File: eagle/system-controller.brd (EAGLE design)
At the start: 99 x 100 mm, 233 parts, among them J1 1, Q0 MOSFET-P-N-PAIR, Q1 MOSFET-P-N-PAIR, Q10 DNP/NTR4101P, Q12 DNP/NTR4101P, Q13 DON3035L, Q2 MOSFET-P-N-PAIR, Q3 MOSFET-P-N-PAIR, Q4 MOSFET-P-N-PAIR, Q5 MOSFET-P-N-PAIR, Q6 MOSFET-P-N-PAIR, Q7 MOSFET-P-N-PAIR, U1 MEGA128-A, U10 TPS25944LRVCRWQFN-20-3X4, U11 TPS25944LRVCRWQFN-20-3X4, U12 TPS25944LRVCRWQFN-20-3X4, U13 TPS25944LRVCRWQFN-20-3X4, U14 TPS25944LRVCRWQFN-20-3X4, U15 TS4100, U2 LP5907MFX-3.0, U3 ACPL-M61L, U4 ACPL-M61L, U5 ACPL-M61L, U6 ACPL-M61L, U7 TPS25944LRVCRWQFN-20-3X4, U8 TPS25944LRVCRWQFN-20-3X4, U9 TPS25944LRVCRWQFN-20-3X4, X1 8 MHz CRYSTAL-ABRACON-ABM3-SMD

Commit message: More board cleanup!
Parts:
- moved TP7GHT 63.7 mm to (78.2, 73.1)
- moved RIMON6 54.5 mm to (85.6, 30.4), turned to 90 degrees
- moved RIMON7 54.2 mm to (85.6, 20.9), turned to 90 degrees
- moved RIMON0 50.1 mm to (85.6, 87.4)
- moved RIMON4 49.9 mm to (85.6, 49.4), turned to 90 degrees
- moved RIMON2 49.0 mm to (85.6, 68.3)
- moved RIMON1 48.6 mm to (85.6, 77.9)
- moved RIMON5 44.8 mm to (85.6, 39.9), turned to 90 degrees
- moved RIMON3 39.7 mm to (85.6, 58.8)
- moved TPLDOA 15.3 mm to (38.9, 76.0)
- moved R60 13.3 mm to (37.2, 75.2), turned to 90 degrees
- moved C22 11.3 mm to (41.9, 76.5), turned to 0 degrees
- moved TP2GHT 9.89 mm to (78.2, 54.2)
- moved TP1GHT 9.82 mm to (77.7, 63.5)
- moved TP5GHT 9.42 mm to (77.3, 24.9)
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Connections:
- net GND: now also CF3.P$19, CF3.P$29, CF3.P$39, CF3.P$9; no longer CF3.P$15, CF3.P$25, CF3.P$35, CF3.P$5
- net VCB1: now also CF3.P$5; no longer CF3.P$9
- net VCB3: now also CF3.P$15; no longer CF3.P$19
- net VCB5: now also CF3.P$25; no longer CF3.P$29
- net VCB7: now also CF3.P$35; no longer CF3.P$39
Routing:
- net VCB7: track 39.0 -> 21.3 mm, vias 2 -> 1
- net V+: track 19.1 -> 8.18 mm, vias 0 -> 2
- net VCB2_IMON: track 68.8 -> 60.0 mm
- net VBUS: track 25.2 -> 16.7 mm, vias 32 -> 48
- net VCB5_IMON: track 70.9 -> 63.1 mm
- net 3V: track 55.9 -> 48.6 mm, vias 30 -> 35
- net GND: track 78.4 -> 71.6 mm, vias 278 -> 279
- net N$48: track 68.8 -> 62.6 mm
- net N$63: track 9.35 -> 3.61 mm
- net N$95: track 9.24 -> 3.61 mm
- net N$79: track 9.15 -> 3.71 mm
- net N$87: track 9.11 -> 3.81 mm
- net N$50: track 9.07 -> 3.81 mm
- net N$49: track 9.04 -> 3.81 mm
- net N$22: track 8.94 -> 3.72 mm
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
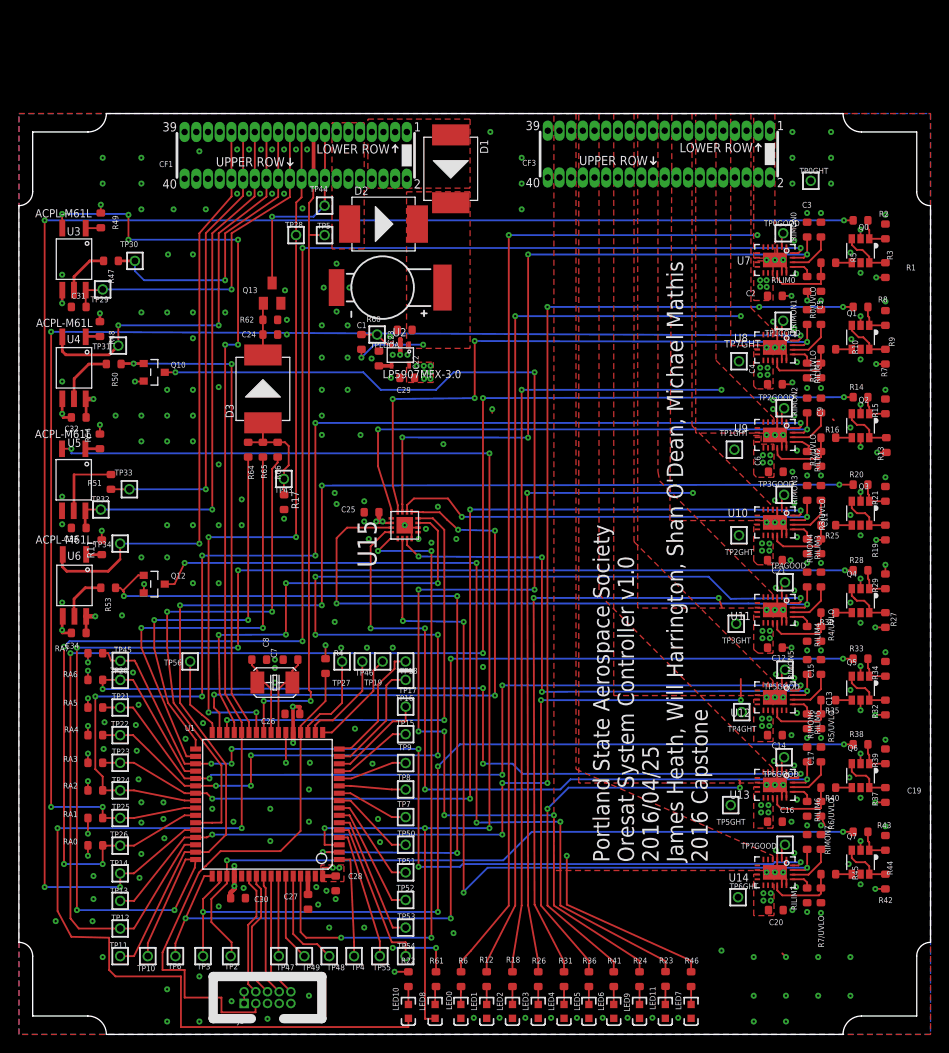
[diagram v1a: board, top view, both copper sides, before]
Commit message: Lots of board cleanup. Improved packages for ATMEGA, analog switch, and TPS. Re-did power polygons to tighten up the layout. Straightened wires because OCD, fixed DRCs.
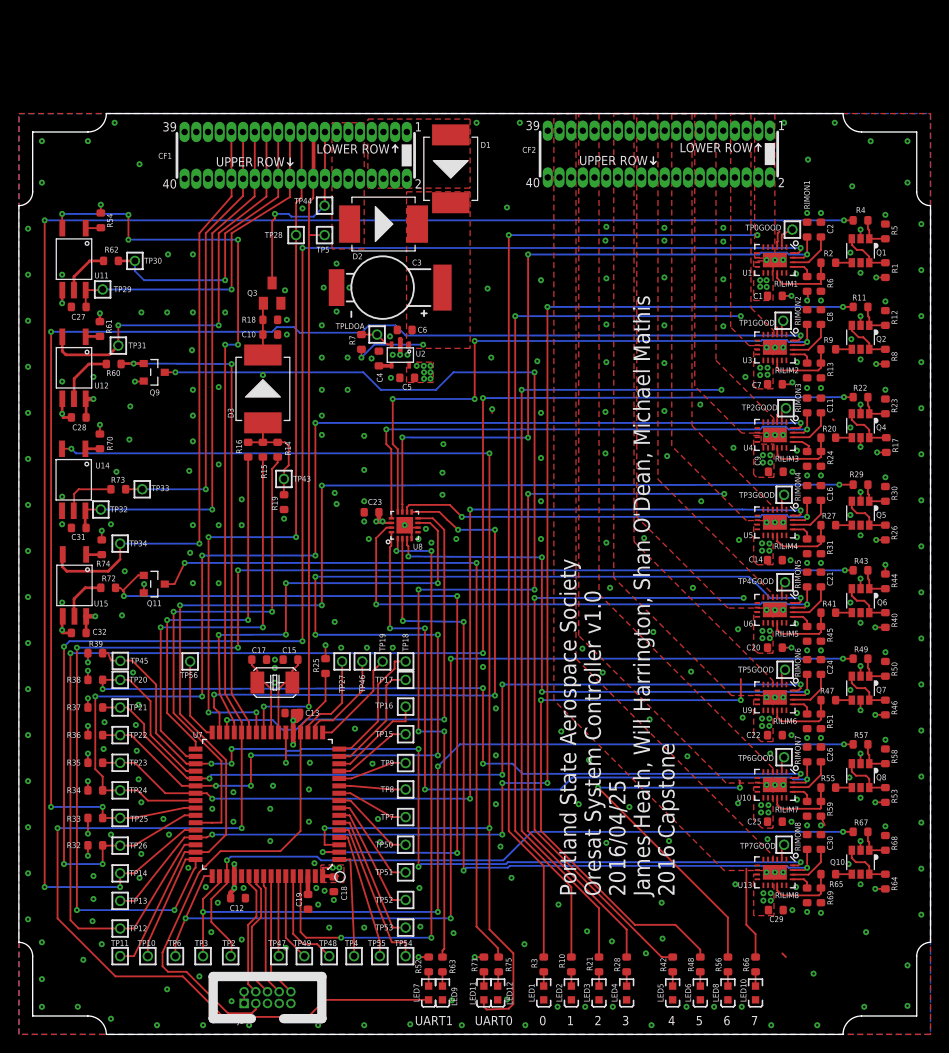
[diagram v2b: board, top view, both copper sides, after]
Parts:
- removed C33, C34: 100nF, rcl_custom:.0603-B-NOSILK
- removed LED0: DNP/GRN, psas_c3_team05:LED-0603
- removed Q0: MOSFET-P-N-PAIR, ic-transistor-mosfet-n-p:SOT23-6
- removed Q13: DON3035L, adafruit:SOT23
- removed R0/UVLO, R1/UVLO, R2/UVLO, R3/UVLO, R4/UVLO, R5/UVLO, RA0, RA1, RA2, RA3, RA4, RA5, RA6, RA7, RILIM0: 47k, rcl_custom:.0603-B-NOSILK
- removed RIMON0: 30k, rcl_custom:.0603-B-NOSILK
- removed TP0GHT, TP1GHT, TP2GHT, TP3GHT, TP4GHT, TP5GHT, TP6GHT, TP7GHT: TEST-POINT, Tova:2MM-TEST-POINT
- added C10: 22u, rcl_custom:.0603-B-NOSILK
- added C18: 100nF, rcl_custom:.0603-B-NOSILK
- added LED12: DNP/AMB, psas_c3_team05:LED-0603
- added Q8: MOSFET-P-N-PAIR, ic-transistor-mosfet-n-p:SOT23-6
- added Q9: DNP/NTR4101P, Tova:SOT23
- added R52, R56, R63, R71, R75: DNP/1k, rcl_custom:.0603-B-NOSILK
- added R55: 93.1k, rcl_custom:.0603-B-NOSILK
- added R57, R67: 4.7k, rcl_custom:.0603-B-NOSILK
- added R58, R68, RILIM8: 47k, rcl_custom:.0603-B-NOSILK
- added R70, R72, R74: 390, rcl_custom:.0603-B-NOSILK
- added R73: 1k, rcl_custom:.0603-B-NOSILK
- added RIMON8: 30k, rcl_custom:.0603-B-NOSILK
- C1: value CAP-ELNA-DS -> 1uF; device cap-elna-ds:CAP-ELNA-DS-SERIES -> rcl_custom:.0603-B-NOSILK
- C12: value 1uF -> 100nF
- C13, C19: value 2.2nF -> 100nF
- C15, C17: value 2.2nF -> 9pF
- C16, C2, C21: value 1uF -> 2.2nF
- C23: value 10nF -> 1uF
- C24: value 22u -> 2.2nF
- C26, C30: value 100nF -> 2.2nF
- C29: value 2.2uF -> 1uF
- C3: value 2.2nF -> CAP-ELNA-DS; device rcl_custom:.0603-B-NOSILK -> cap-elna-ds:CAP-ELNA-DS-SERIES
- C4: value 1uF -> 10nF
- C5: value 2.2nF -> 2.2uF
- C7: value 9pF -> 1uF
- C8: value 9pF -> 2.2nF
- C9: value 2.2nF -> 1uF
- D1, D2: value SMD-DIODE-SCHOTTKY-40V-5A(DO-214AB)-SSC53L -> SSC53L
- LED10, LED8: value DNP/AMB -> DNP/GRN
- LED7: value DNP/GRN -> DNP/AMB
- Q10: value DNP/NTR4101P -> MOSFET-P-N-PAIR; device Tova:SOT23 -> ic-transistor-mosfet-n-p:SOT23-6
- Q3: value MOSFET-P-N-PAIR -> DON3035L; device ic-transistor-mosfet-n-p:SOT23-6 -> adafruit:SOT23
- R10: value 93.1k -> DNP/1k
- R11, R4, R49: value 390 -> 4.7k
- R12, R23, R24, R26, R31, R36, R46, R6: value DNP/1k -> 47k
- R14: value 4.7k -> 390
- R15, R19: value 47k -> 390
- R16, R25: value 93.1k -> 390
- R17, R50, R51, R53, R64: value 390 -> 47k
- R18: value DNP/1k -> 470k
- R2, R20: value 4.7k -> 93.1k
- R21, R3, R42: value 47k -> DNP/1k
- R22: value DNP/1k -> 4.7k
- R27, R9: value 47k -> 93.1k
- R28: value 4.7k -> DNP/1k
- R29: value 47k -> 4.7k
- R30, R35, R40, R45, R5: value 93.1k -> 47k
- R33, R38, R8: value 4.7k -> 47k
- R41: value DNP/1k -> 93.1k
- R47, R65: value 390 -> 93.1k
- R48, R66: value 390 -> DNP/1k
- R60: value 10k -> 390
- R61: value DNP/1k -> 390
- R62: value 470k -> 1k
- R7: value 47k -> 10k
- U1: value MEGA128-A -> TPS25944LRVCRWQFN-20-3X4; device atmegas128:TQFP64 -> system-controller:QFN-20-L
- U11, U12, U14: value TPS25944LRVCRWQFN-20-3X4 -> ACPL-M61L; device system-controller:QFN-20-L -> system-controller:ACPL-M61L
- U15: value TS4100 -> ACPL-M61L; device system-controller:QFN50P400X400X80-17N -> system-controller:ACPL-M61L
- U3, U4, U5, U6: value ACPL-M61L -> TPS25944LRVCRWQFN-20-3X4; device system-controller:ACPL-M61L -> system-controller:QFN-20-L
- U7: value TPS25944LRVCRWQFN-20-3X4 -> ATMEGA128L-8A(U/N); device system-controller:QFN-20-L -> atmegas128:TQFP64
- U8: value TPS25944LRVCRWQFN-20-3X4 -> TS4100; device system-controller:QFN-20-L -> system-controller:QFN50P400X400X80-17N
- moved R49 95.2 mm to (91.4, 40.8), turned to 0 degrees
- moved R48 94.9 mm to (74.0, 7.60), turned to 270 degrees
- moved Q10 93.3 mm to (91.4, 18.7), turned to 0 degrees
- moved R47 91.3 mm to (87.9, 36.3)
- moved R50 90.1 mm to (94.1, 39.7), turned to 90 degrees
- moved R3 87.8 mm to (57.0, 7.60), turned to 270 degrees
- moved R53 87.3 mm to (94.1, 26.0), turned to 90 degrees
- moved U14 87.1 mm to (5.97, 59.9)
- moved R32 87.1 mm to (8.30, 20.5), turned to 0 degrees
- moved R34 86.8 mm to (8.30, 26.5), turned to 0 degrees
- moved R39 86.5 mm to (8.30, 41.4), turned to 0 degrees
- moved R11 86.4 mm to (91.4, 79.0), turned to 0 degrees
- moved R37 86.3 mm to (8.30, 35.5), turned to 0 degrees
- moved R6 85.0 mm to (87.1, 81.5)
- moved U11 85.0 mm to (6.00, 83.9)
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- renumbered CF3 to CF2, Q12 to Q11, R6/UVLO to R59, R7/UVLO to R69
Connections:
- net 3V: now also C12.2, C13.2, C18.2, C23.2, C5.1, Q9.2, R25.1, R32.1, R33.1, R34.1, R35.1, R36.1, R37.1, R38.1, R39.1, R52.1, R61.2, R70.2, R71.1, R74.2, U12.5, U15.5, U7.21, U7.52, U7.64, U8.14; no longer C25.2, C26.2, C29.1, C30.2, C34.2, Q10.2, R11.2, R22.1, R4.1, R48.2, R49.2, R61.1, RA0.1, RA1.1, RA2.1, RA3.1, RA4.1, RA5.1, RA6.1, RA7.1, U1.21, U1.52, U1.64, U15.14, U4.5, U6.5
- net AREF: now also C19.2, U7.62; no longer C27.2, U1.62
- net GND: now also C1.1, C10.2, C13.1, C15.1, C16.2, C17.1, C18.1, C19.1, C2.2, C21.2, C23.1, C26.2, C29.1, C3.-, C30.2, C4.2, C8.2, C9.1, LED10.K, LED12.K, LED8.K, Q10.5, Q3.2, Q8.5, R12.2, R13.2, R18.2, R19.2, R23.2, R24.2, R30.2, R31.2, R45.2, R5.2, R50.2, R51.2, R58.2, R6.2, R68.2, RILIM8.2, RIMON8.2, U1.1, U1.15, U1.16, U1.21, U1.3, U15.3, U3.1, U3.15, U3.16, U3.21, U4.1, U4.15, U4.16, U4.21, U5.1, U5.15, U5.16, U5.21, U6.1, U6.15, U6.16, U6.21, U7.22, U7.53, U7.63, U8.17, U8.4, U8.6; no longer C1.-, C13.2, C15.2, C16.1, C17.2, C19.2, C2.1, C21.1, C23.2, C26.1, C29.2, C3.2, C30.1, C33.1, C34.1, C4.1, C8.1, C9.2, LED0.K, LED11.K, LED7.K, Q0.5, Q13.2, Q3.5, R0/UVLO.2, R1/UVLO.2, R15.2, R17.2, R2/UVLO.2, R21.2, R29.2, R3.2, R3/UVLO.2, R34.2, R39.2, R4/UVLO.2, R5/UVLO.2, R62.2, R9.2, RILIM0.2, RIMON0.2, TP0GHT.1, TP1GHT.1, TP2GHT.1, TP3GHT.1, TP4GHT.1, TP5GHT.1, TP6GHT.1, TP7GHT.1, U1.22, U1.53, U1.63, U11.1, U11.15, U11.16, U11.21, U12.1, U12.15, U12.16, U12.21, U14.1, U14.15, U14.16, U14.21, U15.17, U15.4, U15.6, U7.1, U7.15, U7.16, U7.21, U7.3, U8.1, U8.15, U8.16, U8.21, U8.3
- net I2C-SCL: now also U7.25; no longer U1.25
- net I2C-SDA: now also U7.26; no longer U1.26
- net INOF: now also C2.1, U1.18; no longer C3.1, U7.18
- net N$1: now also C17.2, U7.24; no longer C8.2, U1.24
- net N$10: now also R20.2, R24.1, U4.14; no longer R16.2, R2/UVLO.1, U9.14
- net N$100: now also RILIM7.1, U10.17; no longer RILIM6.1, U13.17
- net N$101: now also U10.2; no longer U13.2
- net N$102: now also C26.1, U10.18; no longer C17.1, U13.18
- net N$103: now also Q8.1, R57.2, R58.1; no longer Q6.1, R38.2, R39.1
- net N$104: now also U7.32; no longer U1.32
- net N$105: now also Q8.3, Q8.6, R53.2; no longer Q6.3, Q6.6, R37.2
- net N$106: now also C10.1, Q3.1, R18.1; no longer C24.1, Q13.1, R62.1
- net N$107: now also U7.61, U8.1; no longer U1.61, U15.1
- net N$108: now also Q7.4, R47.1; no longer Q5.4, R35.1
- net N$109: now also R14.1, R15.1, R16.1, R19.1; no longer R17.1, R64.1, R65.1, R66.1
- net N$11: now also U7.57; no longer U1.57
- net N$110: now also Q10.4, R65.1; no longer Q7.4, R45.1
- net N$111: now also Q8.4, R55.1; no longer Q6.4, R40.1
- net N$12: now also U7.55; no longer U1.55
- net N$13: now also U7.56; no longer U1.56
- net N$14: now also U7.54; no longer U1.54
- net N$15: now also R25.2, U7.20; no longer R4.2, U1.20
- net N$16: now also R73.2, U14.4; no longer R51.2, U5.4
- net N$17: now also C15.2, U7.23; no longer C7.2, U1.23
- net N$18: now also R72.1, U15.4; no longer R53.1, U6.4
- net N$19: now also RILIM3.1, U4.17; no longer RILIM2.1, U9.17
- net N$2: now also Q2.4, R9.1; no longer Q1.4, R10.1
- net N$21: now also RILIM1.1, U1.17; no longer RILIM0.1, U7.17
- net N$22: now also R7.2; no longer R60.2
- net N$23: now also C4.1; no longer C23.1
- net N$24: now also R60.2, U12.4; no longer R50.2, U4.4
- net N$25: now also U1.2; no longer U7.2
- net N$26: now also LED1.A, R3.2; no longer LED0.A, R6.2
- net N$27: now also U7.18; no longer U1.18
- net N$28: now also U7.19; no longer U1.19
- net N$29: now also R13.1, R9.2, U3.14; no longer R1/UVLO.1, R10.2, U8.14
- net N$30: now also RILIM2.1, U3.17; no longer RILIM1.1, U8.17
- net N$32: now also U3.2; no longer U8.2
- net N$33: now also U7.1; no longer U1.1
- net N$34: now also U7.58; no longer U1.58
- net N$35: now also U7.59; no longer U1.59
- net N$37: now also U7.60; no longer U1.60
- net N$38: now also C8.1, U3.18; no longer C5.1, U8.18
- net N$39: now also U7.4; no longer U1.4
- net N$4: now also R70.1, U14.1; no longer R54.1, U5.1
- net N$40: now also U7.5; no longer U1.5
- net N$41: now also U7.6; no longer U1.6
- net N$42: now also U7.7; no longer U1.7
- net N$43: now also U7.8; no longer U1.8
- net N$44: now also U7.9; no longer U1.9
- net N$45: now also LED2.A, R10.2; no longer LED1.A, R12.2
- net N$46: now also U7.29, U8.7; no longer U1.29, U15.7
- net N$47: now also U7.30, U8.8; no longer U1.30, U15.8
- net N$48: now also U7.31, U8.9; no longer U1.31, U15.9
- net N$49: now also Q2.1, R11.2, R12.1; no longer Q1.1, R8.2, R9.1
- net N$5: now also R62.2, U11.4; no longer R47.2, U3.4
- net N$50: now also Q1.1, R4.2, R5.1; no longer Q0.1, R2.2, R3.1
- net N$51: now also Q2.3, Q2.6, R8.2; no longer Q1.3, Q1.6, R7.2
- net N$52: now also LED3.A, R21.2; no longer LED2.A, R18.2
- net N$53: now also LED12.A, R75.2; no longer LED11.A, R23.2
- net N$54: now also R74.1, U15.1; no longer R11.1, U6.1
- net N$55: now also R75.1; no longer R23.1
- net N$56: now also LED7.A, R52.2; no longer LED10.A, R22.2
- net N$57: now also LED11.A, R71.2; no longer LED8.A, R61.2
- net N$58: now also R54.1, U11.1; no longer R49.1, U3.1
- net N$59: now also U4.2; no longer U9.2
- net N$60: now also R63.2; no longer R24.2
- net N$61: now also Q9.3, R63.1; no longer Q10.3, R24.1
- net N$62: now also C11.1, U4.18; no longer C9.1, U9.18
- net N$63: now also Q4.1, R22.2, R23.1; no longer Q2.1, R14.2, R15.1
- net N$64: now also Q4.4, R20.1; no longer Q2.4, R16.1
- net N$65: now also Q4.3, Q4.6, R17.2; no longer Q2.3, Q2.6, R13.2
- net N$66: now also LED4.A, R28.2; no longer LED3.A, R26.2
- net N$67: now also R65.2, U13.14; no longer R45.2, U14.14
- net N$68: now also RILIM8.1, U13.17; no longer RILIM7.1, U14.17
- net N$69: now also U13.2; no longer U14.2
- net N$70: now also C30.1, U13.18; no longer C19.1, U14.18
- net N$71: now also Q10.1, R67.2, R68.1; no longer Q7.1, R43.2, R44.1
- net N$72: now also Q1.3, Q1.6; no longer Q0.3, Q0.6
- net N$73: now also Q10.3, Q10.6, R64.2; no longer Q7.3, Q7.6, R42.2
- net N$74: now also LED5.A, R42.2; no longer LED4.A, R31.2
- net N$75: now also R47.2, R51.1, U9.14; no longer R35.2, R5/UVLO.1, U12.14
- net N$76: now also RILIM6.1, U9.17; no longer RILIM5.1, U12.17
- net N$77: now also U9.2; no longer U12.2
- net N$78: now also C24.1, U9.18; no longer C15.1, U12.18
- net N$79: now also Q7.1, R49.2, R50.1; no longer Q5.1, R33.2, R34.1
- net N$8: now also R61.1, U12.1; no longer R48.1, U4.1
- net N$80: now also Q1.4, R2.1; no longer Q0.4, R5.1
- net N$81: now also Q7.3, Q7.6, R46.2; no longer Q5.3, Q5.6, R32.2
- net N$82: now also LED6.A, R48.2; no longer LED5.A, R36.2
- net N$83: now also R41.2, R45.1, U6.14; no longer R30.2, R4/UVLO.1, U11.14
- net N$84: now also RILIM5.1, U6.17; no longer RILIM4.1, U11.17
- net N$85: now also U6.2; no longer U11.2
- net N$86: now also C21.1, U6.18; no longer C13.1, U11.18
- net N$87: now also Q6.1, R43.2, R44.1; no longer Q4.1, R28.2, R29.1
- net N$88: now also Q5.4, R27.1; no longer Q3.4, R25.1
- net N$89: now also Q6.3, Q6.6, R40.2; no longer Q4.3, Q4.6, R27.2
- net N$9: now also R2.2, R6.1, U1.14; no longer R0/UVLO.1, R5.2, U7.14
- net N$90: now also LED8.A, R56.2; no longer LED6.A, R41.2
- net N$91: now also R27.2, R31.1, U5.14; no longer R25.2, R3/UVLO.1, U10.14
- net N$92: now also RILIM4.1, U5.17; no longer RILIM3.1, U10.17
- net N$93: now also U5.2; no longer U10.2
- net N$94: now also C16.1, U5.18; no longer C11.1, U10.18
- net N$95: now also Q5.1, R29.2, R30.1; no longer Q3.1, R20.2, R21.1
- net N$96: now also Q6.4, R41.1; no longer Q4.4, R30.1
- net N$97: now also Q5.3, Q5.6, R26.2; no longer Q3.3, Q3.6, R19.2
- net N$98: now also LED10.A, R66.2; no longer LED7.A, R46.2
- net N$99: now also R55.2, U10.14; no longer R40.2, U13.14
- net NUCLEAROPTION0: now also R16.2, U7.33; no longer R64.2, U1.33
- net NUCLEAROPTION1: now also R15.2, U7.34; no longer R65.2, U1.34
- net NUCLEAROPTION2: now also R14.2, U7.43; no longer R66.2, U1.43
- net NUCLEAROPTION_OUT: now also Q3.3; no longer Q13.3
- net PB0: now also U7.10; no longer U1.10
- net PB1: now also U7.11; no longer U1.11
- net PB2: now also U7.12; no longer U1.12
- net PB3: now also U7.13; no longer U1.13
- net PB4: now also U7.14; no longer U1.14
- net PB5: now also U7.15; no longer U1.15
- net PB6: now also U7.16; no longer U1.16
- net PB7: now also U7.17; no longer U1.17
- net PCB3_EN: now also R29.1, U7.47; no longer R20.1, U1.47
- net RXD0: now also R72.2, U7.2; no longer R53.2, U1.2
- net RXD1: now also Q9.1, R60.1, U7.27; no longer Q10.1, R50.1, U1.27
- net TXD0: now also LED11.K, U14.2, U7.3; no longer LED8.K, U1.3, U5.2
- net TXD1: now also LED7.K, U11.2, U7.28; no longer LED10.K, U1.28, U3.2
- net UART_FC_RX: now also R62.1; no longer R47.1
- net UART_FC_TX: now also U12.2; no longer U4.2
- net UART_FC_VCC: now also C27.2, U11.5; no longer C31.2, U3.5
- net UART_LGR_RX: now also R73.1; no longer R51.1
- net UART_LGR_TX: now also U15.2; no longer U6.2
- net UART_LGR_VCC: now also C31.2, U14.5; no longer C33.2, U5.5
- net V+: now also C3.+, C6.2, R7.1; no longer C1.+, C22.2, R60.1
- net VBUS: now also C1.2, C22.2, C25.2, C29.2, C7.2, C9.2, Q10.2, Q8.2, R17.1, R26.1, R40.1, R46.1, R53.1, R64.1, R8.1, U1.10, U1.11, U1.12, U1.13, U1.9, U3.10, U3.11, U3.12, U3.13, U3.9, U4.10, U4.11, U4.12, U4.13, U4.9, U5.10, U5.11, U5.12, U5.13, U5.9, U6.10, U6.11, U6.12, U6.13, U6.9; no longer C12.2, C16.2, C2.2, C21.2, C4.2, C6.2, Q0.2, Q3.2, R13.1, R19.1, R27.1, R32.1, R37.1, R42.1, R7.1, U11.10, U11.11, U11.12, U11.13, U11.9, U12.10, U12.11, U12.12, U12.13, U12.9, U14.10, U14.11, U14.12, U14.13, U14.9, U7.10, U7.11, U7.12, U7.13, U7.9, U8.10, U8.11, U8.12, U8.13, U8.9
- net VCB0: now also R3.1, U1.4, U1.5, U1.6, U1.7, U1.8; no longer R6.1, U7.4, U7.5, U7.6, U7.7, U7.8
- net VCB0_!FLT: now also R32.2, U1.20, U7.42; no longer RA0.2, U1.42, U7.20
- net VCB0_EN: now also R4.1, U7.44; no longer R2.1, U1.44
- net VCB0_IMON: now also RIMON1.1, U1.19, U8.11; no longer RIMON0.1, U15.11, U7.19
- net VCB1: now also R10.1, U3.4, U3.5, U3.6, U3.7, U3.8; no longer R12.1, U8.4, U8.5, U8.6, U8.7, U8.8
- net VCB1_!FLT: now also R33.2, U3.20, U7.41; no longer RA1.2, U1.41, U8.20
- net VCB1_EN: now also R11.1, U7.45; no longer R8.1, U1.45
- net VCB1_IMON: now also RIMON2.1, U3.19, U8.12; no longer RIMON1.1, U15.12, U8.19
- net VCB2: now also R21.1, U4.4, U4.5, U4.6, U4.7, U4.8; no longer R18.1, U9.4, U9.5, U9.6, U9.7, U9.8
- net VCB2_!FLT: now also R34.2, U4.20, U7.40; no longer RA2.2, U1.40, U9.20
- net VCB2_EN: now also R22.1, U7.46; no longer R14.1, U1.46
- net VCB2_IMON: now also RIMON3.1, U4.19, U8.13; no longer RIMON2.1, U15.13, U9.19
- net VCB3: now also R28.1, U5.4, U5.5, U5.6, U5.7, U5.8; no longer R26.1, U10.4, U10.5, U10.6, U10.7, U10.8
- net VCB3_!FLT: now also R35.2, U5.20, U7.39; no longer RA3.2, U1.39, U10.20
- net VCB3_IMON: now also RIMON4.1, U5.19, U8.10; no longer RIMON3.1, U10.19, U15.10
- net VCB4: now also R42.1, U6.4, U6.5, U6.6, U6.7, U6.8; no longer R31.1, U11.4, U11.5, U11.6, U11.7, U11.8
- net VCB4_!FLT: now also R36.2, U6.20, U7.38; no longer RA4.2, U1.38, U11.20
- net VCB4_EN: now also R43.1, U7.48; no longer R28.1, U1.48
- net VCB4_IMON: now also RIMON5.1, U6.19, U8.15; no longer RIMON4.1, U11.19, U15.15
- net VCB5: now also R48.1, U9.4, U9.5, U9.6, U9.7, U9.8; no longer R36.1, U12.4, U12.5, U12.6, U12.7, U12.8
- net VCB5_!FLT: now also R37.2, U7.37, U9.20; no longer RA5.2, U1.37, U12.20
- net VCB5_EN: now also R49.1, U7.49; no longer R33.1, U1.49
- net VCB5_IMON: now also RIMON6.1, U8.3, U9.19; no longer RIMON5.1, U12.19, U15.3
- net VCB6: now also R56.1, U10.4, U10.5, U10.6, U10.7, U10.8; no longer R41.1, U13.4, U13.5, U13.6, U13.7, U13.8
- net VCB6_!FLT: now also R38.2, U10.20, U7.36; no longer RA6.2, U1.36, U13.20
- net VCB6_EN: now also R57.1, U7.50; no longer R38.1, U1.50
- net VCB6_IMON: now also RIMON7.1, U10.19, U8.16; no longer RIMON6.1, U13.19, U15.16
- net VCB7: now also R66.1, U13.4, U13.5, U13.6, U13.7, U13.8; no longer R46.1, U14.4, U14.5, U14.6, U14.7, U14.8
- net VCB7_!FLT: now also R39.2, U13.20, U7.35; no longer RA7.2, U1.35, U14.20
- net VCB7_EN: now also R67.1, U7.51; no longer R43.1, U1.51
- net VCB7_IMON: now also RIMON8.1, U13.19, U8.2; no longer RIMON7.1, U14.19, U15.2
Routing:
- net GND: track 71.6 -> 32.5 mm, vias 279 -> 357
- net N$61: track 139.2 -> 120.7 mm, vias 8 -> 6
- net N$55: track 95.8 -> 79.1 mm, vias 4 -> 2
- net VCB7: track 21.3 -> 10.0 mm, vias 1 -> 0
- net VCB4_IMON: track 68.3 -> 60.0 mm
- net VCB5: track 55.4 -> 61.6 mm
- net VCB4: track 62.6 -> 68.6 mm
- net VCB3: track 70.1 -> 76.0 mm
- net 3V: track 48.6 -> 44.0 mm, vias 35 -> 34
- net TXD1: track 168.3 -> 164.6 mm
- net VCB7_IMON: track 87.3 -> 83.8 mm
- net N$107: track 71.1 -> 67.7 mm
- net VCB6: track 43.7 -> 40.5 mm
- net VCB6_IMON: track 80.9 -> 77.6 mm
- net N$15: track 58.3 -> 55.3 mm
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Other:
- board text added: "0"
- board text added: "1"
- board text added: "2"
- board text added: "3"
- board text added: "4"
- board text added: "5"
- board text added: "6"
- board text added: "7"
- board text added: "UART0"
- board text added: "UART1"

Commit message: Added 3V LED for power. Fixed a DRC error which wasn't caught earlier? How'd that happen? Also pushing gerbers, since some folks don't have EAGLE.
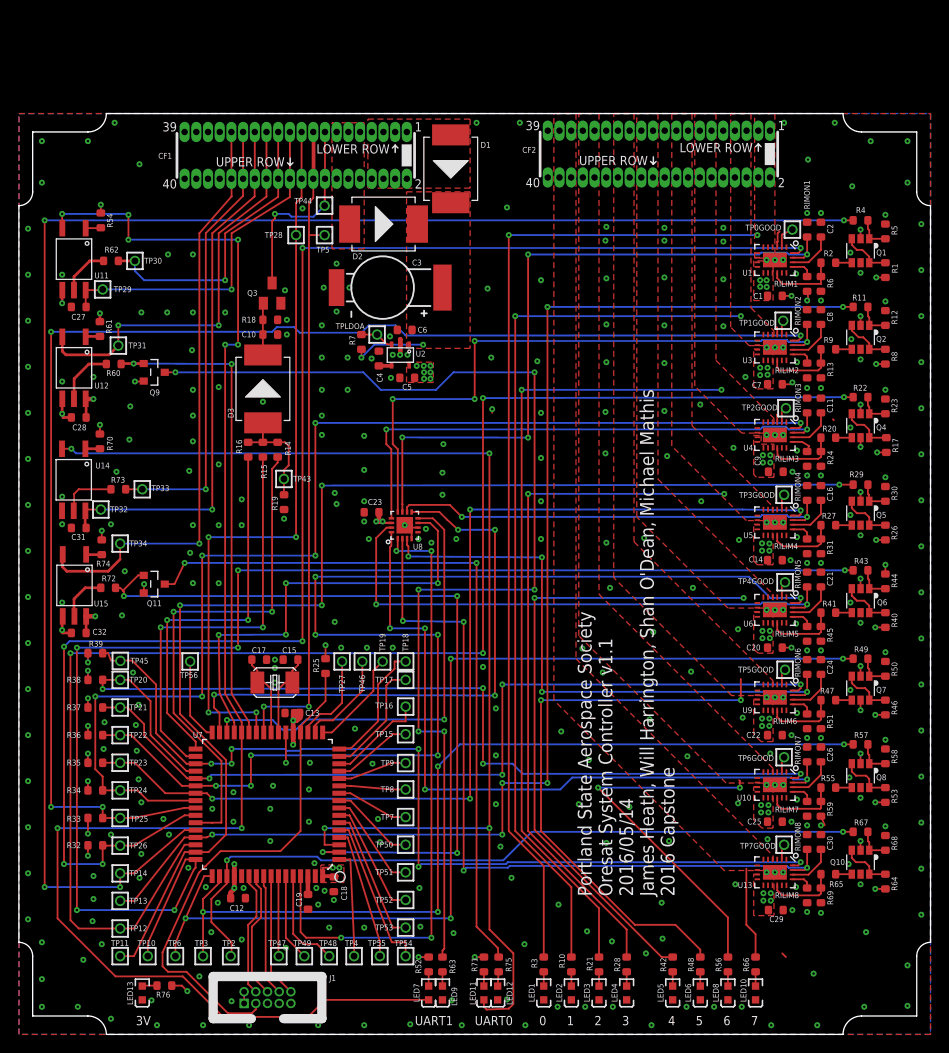
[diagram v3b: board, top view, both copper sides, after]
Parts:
- added LED13: DNP/GRN, psas_c3_team05:LED-0603
- added R76: DNP/1k, rcl_custom:.0603-B-NOSILK
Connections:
- new net N$6: LED13.A, R76.2
- net 3V: now also R76.1
- net GND: now also LED13.K
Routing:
- net 3V: track 44.0 -> 46.7 mm, vias 34 -> 35
- net N$6: track 0.00 -> 1.62 mm
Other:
- board text added: "3V"
- board text added: "Portland State Aerospace Society Oresat System Controller v1.1 2016/05/14 James Heath, Will Harrington, Shan O'Dean, Michael Mathis 2016 Capstone"
- board text removed: "Portland State Aerospace Society Oresat System Controller v1.0 2016/04/25 James Heath, Will Harrington, Shan O'Dean, Michael Mathis 2016 Capstone"
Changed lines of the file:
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@@
 <layers>
 <layer number="1" name="Top" color="4" fill="1" visible="yes" active="yes"/>
-<layer number="2" name="Route2" color="15" fill="1" visible="no" active="yes"/>
+<layer number="2" name="Route2" color="15" fill="1" visible="yes" active="yes"/>
 <layer number="3" name="Route3" color="4" fill="3" visible="no" active="no"/>
 <layer number="4" name="Route4" color="1" fill="4" visible="no" active="no"/>
@@
 <layer number="13" name="Route13" color="4" fill="5" visible="no" active="no"/>
 <layer number="14" name="Route14" color="1" fill="6" visible="no" active="no"/>
-<layer number="15" name="Route15" color="14" fill="1" visible="no" active="yes"/>
-<layer number="16" name="Bottom" color="1" fill="1" visible="no" active="yes"/>
+<layer number="15" name="Route15" color="14" fill="1" visible="yes" active="yes"/>
+<layer number="16" name="Bottom" color="1" fill="1" visible="yes" active="yes"/>
 <layer number="17" name="Pads" color="2" fill="1" visible="yes" active="yes"/>
 <layer number="18" name="Vias" color="2" fill="1" visible="yes" active="yes"/>
@@
 <layer number="23" name="tOrigins" color="15" fill="1" visible="yes" active="yes"/>
 <layer number="24" name="bOrigins" color="15" fill="1" visible="no" active="yes"/>
-<layer number="25" name="tNames" color="7" fill="1" visible="no" active="yes"/>
+<layer number="25" name="tNames" color="7" fill="1" visible="yes" active="yes"/>
 <layer number="26" name="bNames" color="7" fill="1" visible="no" active="yes"/>
 <layer number="27" name="tValues" color="7" fill="1" visible="no" active="yes"/>
@@
 <board>
 <plain>
-<text x="71.2" y="15" size="1.778" layer="21" rot="R90">Portland State Aerospace Society
-Oresat System Controller v1.0
-2016/04/25
+<text x="71.2" y="15" size="1.5" layer="21" font="vector" ratio="10" rot="R90">Portland State Aerospace Society
+Oresat System Controller v1.1
+2016/05/14
 James Heath, Will Harrington, Shan O'Dean, Michael Mathis
 2016 Capstone</text>
@@
 <circle x="81.2" y="84.1" radius="0.3" width="0" layer="30"/>
 <circle x="41.9" y="55.3" radius="0.3" width="0" layer="30"/>
+<text x="12.7" y="1" size="1" layer="21" font="vector" ratio="15">3V</text>
 </plain>
 <attributes>
@@
 <attribute name="MFN" value="CNC Tech" x="27" y="4" size="1.778" layer="27" display="off"/>
 <attribute name="MPN" value="3220-10-0100-00" x="27" y="4" size="1.778" layer="27" display="off"/>
-<attribute name="NAME" x="23.72" y="1.165" size="0.635" layer="25" font="vector" ratio="20"/>
+<attribute name="NAME" x="33.7" y="5.8" size="0.635" layer="25" font="vector" ratio="20"/>
 <attribute name="VALUE" x="22.3" y="1" size="0.635" layer="27" font="vector" ratio="15" align="top-left"/>
 </element>
@@
 <attribute name="NAME" x="28.8" y="57.8" size="0.3" layer="33" ratio="15" rot="R270" align="center"/>
 </element>
+<element name="R76" library="rcl_custom" package=".0603-B-NOSILK" value="DNP/1k" x="15.8" y="5.3" smashed="yes" rot="R180">
+<attribute name="MFN" value="Samsung" x="15.8" y="5.3" size="1.778" layer="27" rot="R180" display="off"/>
+<attribute name="DIST" value="digikey" x="15.8" y="5.3" size="1.778" layer="27" rot="R180" display="off"/>
+<attribute name="MPN" value="RC1608F102CS" x="15.8" y="5.3" size="1.778" layer="27" rot="R180" display="off"/>
+<attribute name="DPN" value="1276-3484-1-ND" x="15.8" y="5.3" size="1.778" layer="27" rot="R180" display="off"/>
+<attribute name="NAME" x="14.9" y="4" size="0.635" layer="25" font="vector" ratio="20"/>
+<attribute name="VALUE" x="17" y="6.9" size="0.8" layer="27" font="vector" ratio="15" rot="R180"/>
+<attribute name="NAME" x="15.8" y="5.3" size="0.3" layer="33" ratio="15" rot="R180" align="center"/>
+</element>
+<element name="LED13" library="psas_c3_team05" package="LED-0603" value="DNP/GRN" x="13.4" y="4.5" smashed="yes" rot="R90">
+<attribute name="MFN" value="Wurth Electronics INC." x="13.4" y="4.5" size="1.778" layer="27" rot="R90" display="off"/>
+<attribute name="DIST" value="digikey" x="13.4" y="4.5" size="1.778" layer="27" rot="R90" display="off"/>
+<attribute name="MPN" value="150060GS75000" x="13.4" y="4.5" size="1.778" layer="27" rot="R90" display="off"/>
+<attribute name="DPN" value="732-4971-1-ND" x="13.4" y="4.5" size="1.778" layer="27" rot="R90" display="off"/>
+<attribute name="NAME" x="12.4" y="3.2" size="0.635" layer="25" font="vector" ratio="20" rot="R90"/>
+<attribute name="VALUE" x="15.45" y="3" size="1" layer="27" font="vector" ratio="10" rot="R90"/>
+</element>
 </elements>
 <signals>
@@
 <wire x1="29.79" y1="34.09" x2="29.79" y2="35.1" width="0.5" layer="1"/>
 <wire x1="29.79" y1="35.1" x2="30.6" y2="35.1" width="0.5" layer="1"/>
+<contactref element="R76" pad="1"/>
+<wire x1="16.6" y1="5.3" x2="17.7" y2="5.3" width="0.2" layer="1"/>
+<wire x1="17.7" y1="5.3" x2="18.3" y2="4.7" width="0.2" layer="1"/>
+<via x="18.3" y="4.7" extent="1-16" drill="0.254"/>
+<wire x1="18.3" y1="4.7" x2="18.3" y2="4.1" width="0.2" layer="15"/>
+<wire x1="18.3" y1="4.1" x2="18.4" y2="4" width="0.2" layer="15"/>
 </signal>
 <signal name="N$26">
@@
 <via x="9" y="9.8" extent="1-16" drill="0.254"/>
 <via x="15" y="1" extent="1-16" drill="0.254"/>
-<via x="16.1" y="4.9" extent="1-16" drill="0.254"/>
+<via x="14.4" y="3.7" extent="1-16" drill="0.254"/>
 <via x="19.6" y="6.3" extent="1-16" drill="0.254"/>
 <via x="37.5" y="11.6" extent="1-16" drill="0.254"/>
@@
 <via x="85.7" y="95" extent="1-16" drill="0.254"/>
 <via x="32.1" y="18.6" extent="1-16" drill="0.254"/>
-<via x="26.5" y="71.6" extent="1-16" drill="0.254"/>
+<via x="26.5" y="68.7" extent="1-16" drill="0.254"/>
+<contactref element="LED13" pad="K"/>
 </signal>
 <signal name="N$207">
@@
 <wire x1="7.305" y1="52.195" x2="7.4" y2="52.1" width="0.2" layer="1"/>
 </signal>
+<signal name="N$6">
+<contactref element="R76" pad="2"/>
+<contactref element="LED13" pad="A"/>
+<wire x1="15" y1="5.3" x2="13.45" y2="5.3" width="0.2" layer="1"/>
+<wire x1="13.45" y1="5.3" x2="13.4" y2="5.25" width="0.2" layer="1"/>
+</signal>
 </signals>

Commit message: Updating resitor and capacitor names
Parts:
- R60, R72: value 390 -> 0 Ohm
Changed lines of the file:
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@@
 <attribute name="NAME" x="6.5" y="67" size="0.3" layer="33" ratio="15" align="center"/>
 </element>
-<element name="R60" library="rcl_custom" package=".0603-B-NOSILK" value="390" x="10.3" y="72.8" smashed="yes" rot="R180">
+<element name="R60" library="rcl_custom" package=".0603-B-NOSILK" value="0 Ohm" x="10.3" y="72.8" smashed="yes" rot="R180">
 <attribute name="DIST" value="digikey" x="10.3" y="72.8" size="1.778" layer="27" rot="R180" display="off"/>
 <attribute name="MFN" value="TE " x="10.3" y="72.8" size="1.778" layer="27" rot="R180" display="off"/>
@@
 <attribute name="NAME" x="8.8" y="64.4" size="0.3" layer="33" ratio="15" rot="R90" align="center"/>
 </element>
-<element name="R72" library="rcl_custom" package=".0603-B-NOSILK" value="390" x="9.7" y="48.5" smashed="yes">
+<element name="R72" library="rcl_custom" package=".0603-B-NOSILK" value="0 Ohm" x="9.7" y="48.5" smashed="yes">
 <attribute name="DIST" value="digikey" x="9.7" y="48.5" size="1.778" layer="27" display="off"/>
 <attribute name="MFN" value="TE " x="9.7" y="48.5" size="1.778" layer="27" display="off"/>
